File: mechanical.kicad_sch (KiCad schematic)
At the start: 12 parts

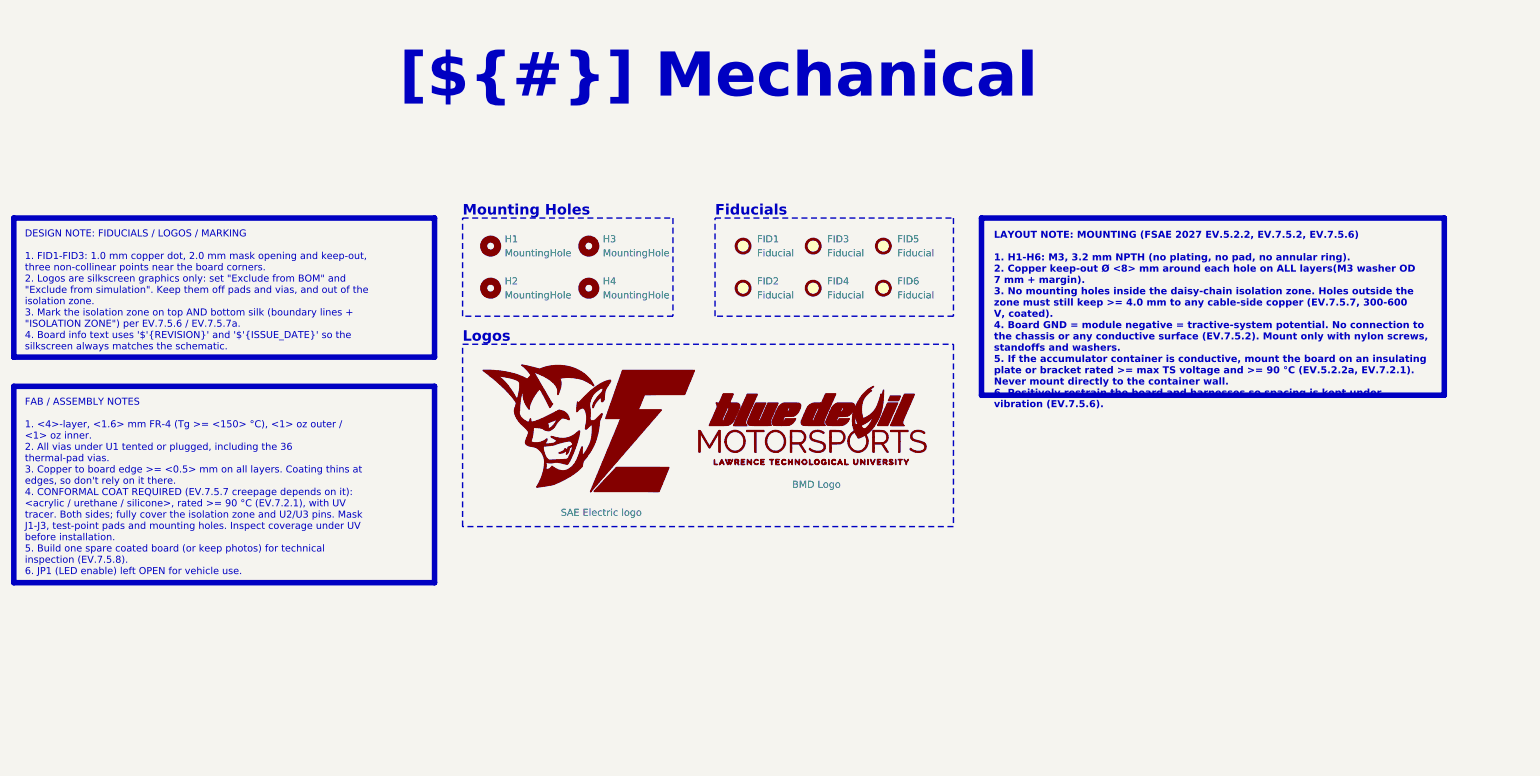
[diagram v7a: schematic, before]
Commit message: PCB[Trace Size, Testpad, Daisy]: Changed Bat Trace size FAT, Made test pads larger, small trace movement to clean up, daisy trace change. SCH[Notes]: Small notes changes.
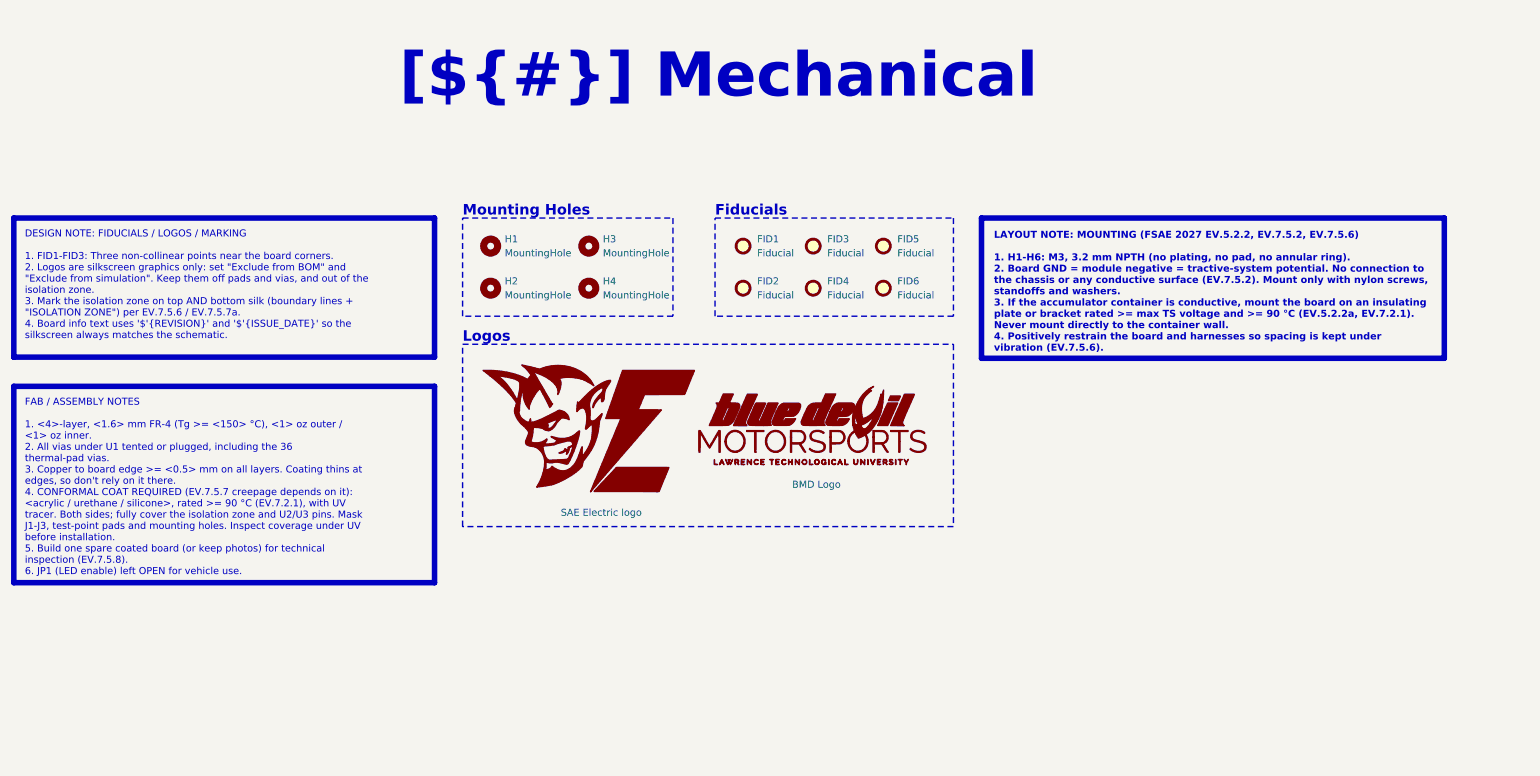
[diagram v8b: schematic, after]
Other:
- company: (none) -> ${COMPANY}
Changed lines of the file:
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@@
 	(title_block
 		(title "Mechanical")
+		(date "2026-10-28")
+		(rev "${REVISION}")
+		(company "${COMPANY}")
 	)
 	(rectangle
@@
 		)
 	)
-	(text_box "LAYOUT NOTE: MOUNTING (FSAE 2027 EV.5.2.2, EV.7.5.2, EV.7.5.6)\n\n1. H1-H6: M3, 3.2 mm NPTH (no plating, no pad, no annular ring).\n2. Copper keep-out Ø <8> mm around each hole on ALL layers(M3 washer OD 7 mm + margin).\n3. No mounting holes inside the daisy-chain isolation zone. Holes outside the zone must still keep >= 4.0 mm to any cable-side copper (EV.7.5.7, 300-600 V, coated).\n4. Board GND = module negative = tractive-system potential. No connection to the chassis or any conductive surface (EV.7.5.2). Mount only with nylon screws, standoffs and washers.\n5. If the accumulator container is conductive, mount the board on an insulating plate or bracket rated >= max TS voltage and >= 90 °C (EV.5.2.2a, EV.7.2.1). Never mount directly to the container wall.\n6. Positively restrain the board and harnesses so spacing is kept under vibration (EV.7.5.6)."
+	(text_box "LAYOUT NOTE: MOUNTING (FSAE 2027 EV.5.2.2, EV.7.5.2, EV.7.5.6)\n\n1. H1-H6: M3, 3.2 mm NPTH (no plating, no pad, no annular ring).\n2. Board GND = module negative = tractive-system potential. No connection to the chassis or any conductive surface (EV.7.5.2). Mount only with nylon screws, standoffs and washers.\n3. If the accumulator container is conductive, mount the board on an insulating plate or bracket rated >= max TS voltage and >= 90 °C (EV.5.2.2a, EV.7.2.1). Never mount directly to the container wall.\n4. Positively restrain the board and harnesses so spacing is kept under vibration (EV.7.5.6)."
 		(exclude_from_sim no)
 		(at 195.58 50.8 0)
-		(size 83.82 32.0932)
+		(size 83.82 25.4)
 		(margins 2.25 2.25 2.25 2.25)
 		(stroke
@@
 		)
 	)
-	(text_box "DESIGN NOTE: FIDUCIALS / LOGOS / MARKING\n\n1. FID1-FID3: 1.0 mm copper dot, 2.0 mm mask opening and keep-out, three non-collinear points near the board corners.\n2. Logos are silkscreen graphics only: set \"Exclude from BOM\" and \"Exclude from simulation\". Keep them off pads and vias, and out of the isolation zone.\n3. Mark the isolation zone on top AND bottom silk (boundary lines + \"ISOLATION ZONE\") per EV.7.5.6 / EV.7.5.7a.\n4. Board info text uses '$'{REVISION}' and '$'{ISSUE_DATE}' so the silkscreen always matches the schematic."
+	(text_box "DESIGN NOTE: FIDUCIALS / LOGOS / MARKING\n\n1. FID1-FID3: Three non-collinear points near the board corners.\n2. Logos are silkscreen graphics only: set \"Exclude from BOM\" and \"Exclude from simulation\". Keep them off pads and vias, and out of the isolation zone.\n3. Mark the isolation zone on top AND bottom silk (boundary lines + \"ISOLATION ZONE\") per EV.7.5.6 / EV.7.5.7a.\n4. Board info text uses '$'{REVISION}' and '$'{ISSUE_DATE}' so the silkscreen always matches the schematic."
 		(exclude_from_sim no)
 		(at 20.32 50.8 0)
